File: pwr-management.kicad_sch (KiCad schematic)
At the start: 3 parts, among them U3 BQ297xy, U4 BQ25176JDSGR

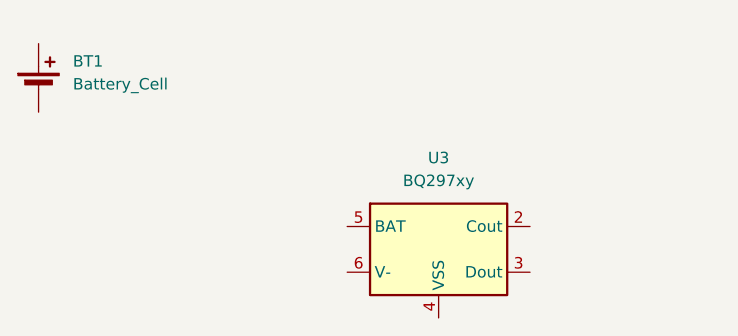
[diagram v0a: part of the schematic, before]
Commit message: component placement inside schematic
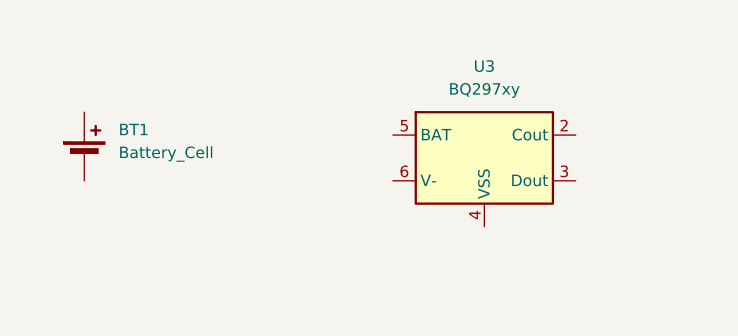
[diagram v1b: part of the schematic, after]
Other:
- moved on the sheet: BT1, U3
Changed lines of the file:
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@@
 	(symbol
 		(lib_id "Battery_Management:BQ297xy")
-		(at 88.9 91.44 0)
+		(at 93.98 81.28 0)
 		(unit 1)
 		(exclude_from_sim no)
@@
 		(fields_autoplaced yes)
 		(property "Reference" "U3"
-			(at 88.9 81.28 0)
+			(at 93.98 71.12 0)
 			(effects
 				(font
@@
 		)
 		(property "Value" "BQ297xy"
-			(at 88.9 83.82 0)
+			(at 93.98 73.66 0)
 			(effects
 				(font
@@
 		)
 		(property "Footprint" "Package_SON:WSON-6_1.5x1.5mm_P0.5mm"
-			(at 88.9 82.55 0)
+			(at 93.98 72.39 0)
 			(effects
 				(font
@@
 		)
 		(property "Datasheet" "http://www.ti.com/lit/ds/symlink/bq2970.pdf"
-			(at 82.55 86.36 0)
+			(at 87.63 76.2 0)
 			(effects
 				(font
@@
 		)
 		(property "Description" "Voltage and Current Protection for Single-Cell Li-Ion and Li-Polymer Batteries"
-			(at 88.9 91.44 0)
+			(at 93.98 81.28 0)
 			(effects
 				(font
@@
 	(symbol
 		(lib_id "Device:Battery_Cell")
-		(at 44.45 73.66 0)
+		(at 49.53 81.28 0)
 		(unit 1)
 		(exclude_from_sim no)
@@
 		(fields_autoplaced yes)
 		(property "Reference" "BT1"
-			(at 48.26 70.5484 0)
+			(at 53.34 78.1684 0)
 			(effects
 				(font
@@
 		)
 		(property "Value" "Battery_Cell"
-			(at 48.26 73.0884 0)
+			(at 53.34 80.7084 0)
 			(effects
 				(font
@@
 		)
 		(property "Footprint" ""
-			(at 44.45 72.136 90)
+			(at 49.53 79.756 90)
 			(effects
 				(font
@@
 		)
 		(property "Datasheet" "~"
-			(at 44.45 72.136 90)
+			(at 49.53 79.756 90)
 			(effects
 				(font
@@
 		)
 		(property "Description" "Single-cell battery"
-			(at 44.45 73.66 0)
+			(at 49.53 81.28 0)
 			(effects
 				(font

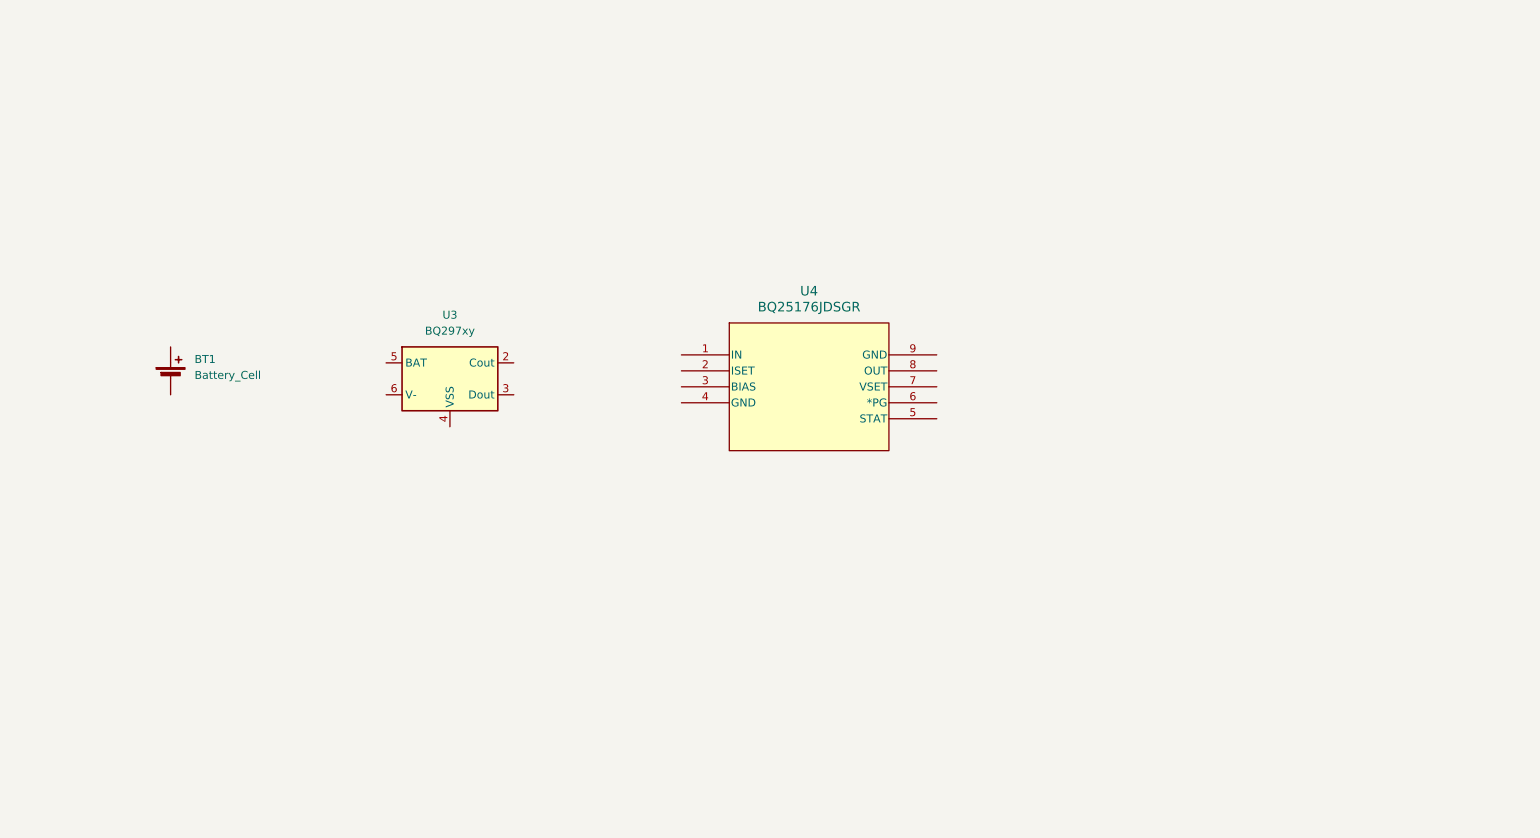
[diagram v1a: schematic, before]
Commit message: fix BQ25176J library
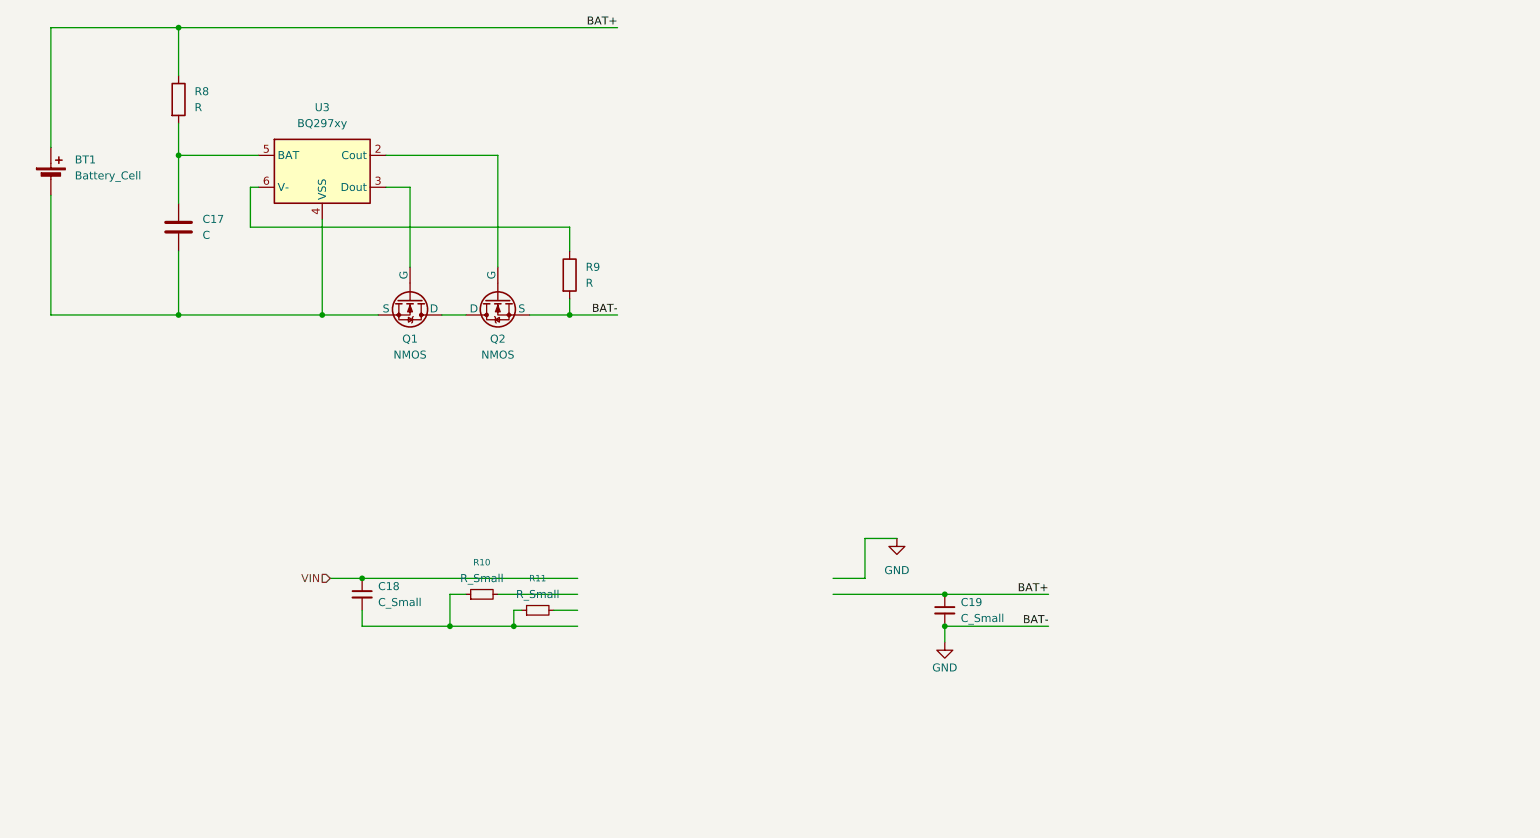
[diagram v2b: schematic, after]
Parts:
- removed U4: BQ25176JDSGR, WSON_MDSGR_TEX, symbol 2025-10-25_14-37-11:BQ25176JDSGR
- added C17: C, symbol Device:C
- added C18, C19: C_Small, symbol Device:C_Small
- added Q1, Q2: NMOS, symbol Simulation_SPICE:NMOS
- added R10, R11: R_Small, symbol Device:R_Small
- added R8, R9: R, symbol Device:R
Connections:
- net at U3.2 (Cout): now also Q2.2 (G)
- net at U3.3 (Dout): now also Q1.2 (G)
- net at U3.4 (VSS): now also BT1.2 (-), C17.2, Q1.3 (S)
- net at U3.5 (BAT): now also C17.1, R8.2
- net at U3.6 (V-): now also R9.1
- net BAT+: now reaches BT1.1 (+)
- net BAT+: now also C19.1, R8.1
- new net: C18.2, R10.1, R11.1
- new net: Q1.1 (D), Q2.1 (D)
- new net GND: C19.2, Q2.3 (S), R9.2
- new net VIN: C18.1
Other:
- moved on the sheet: BT1, U3

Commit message: Add battery handling
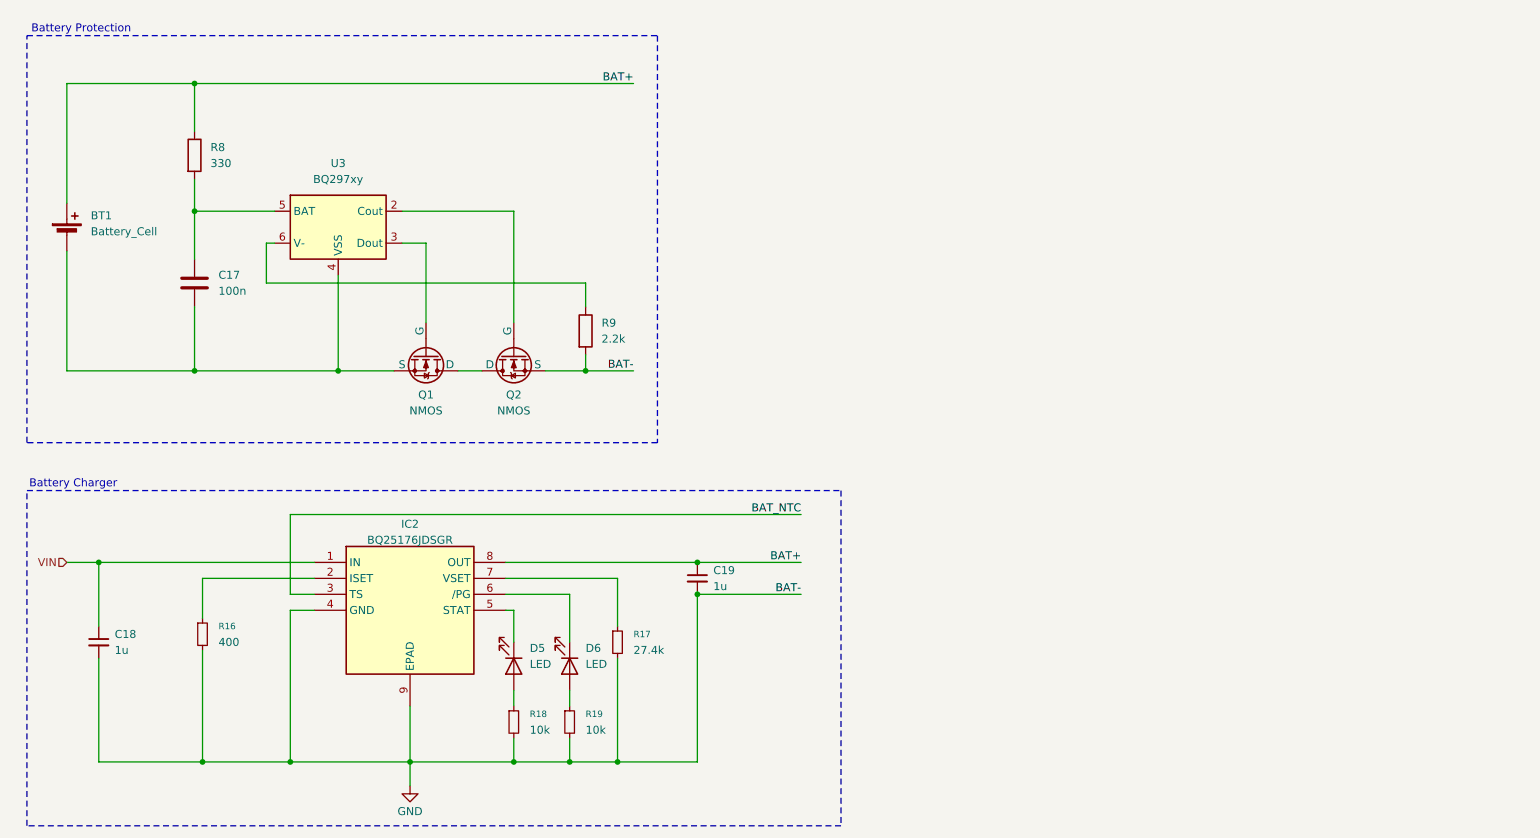
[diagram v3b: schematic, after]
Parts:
- removed R10, R11: R_Small, symbol Device:R_Small
- added D5, D6: LED, symbol Device:LED
- added IC2: BQ25176JDSGR, SON50P200X200X80-9N, symbol BQ25176J:BQ25176JDSGR
- added R16: 400, symbol Device:R_Small
- added R17: 27.4k, symbol Device:R_Small
- added R18, R19: 10k, symbol Device:R_Small
- C17: value C -> 100n
- C18, C19: value C_Small -> 1u
- R8: value R -> 330
- R9: value R -> 2.2k
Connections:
- net BAT+: now also IC2.8 (OUT)
- net GND: now also C18.2, IC2.4 (GND), IC2.9 (EPAD), R16.2, R17.2, R18.2, R19.2
- net VIN: now also IC2.1 (IN)
- new net: IC2.2 (ISET), R16.1
- new net: D5.1 (K), IC2.5 (STAT)
- new net: D6.1 (K), IC2.6 (/PG)
- new net: IC2.7 (VSET), R17.1
- new net: D5.2 (A), R18.1
- new net: D6.2 (A), R19.1
- new net BAT_NTC: IC2.3 (TS)
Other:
- note added: "Battery Charger"
- note added: "Battery Protection"
- moved on the sheet: BT1, C17, C18, C19, Q1, Q2, R8, R9, U3

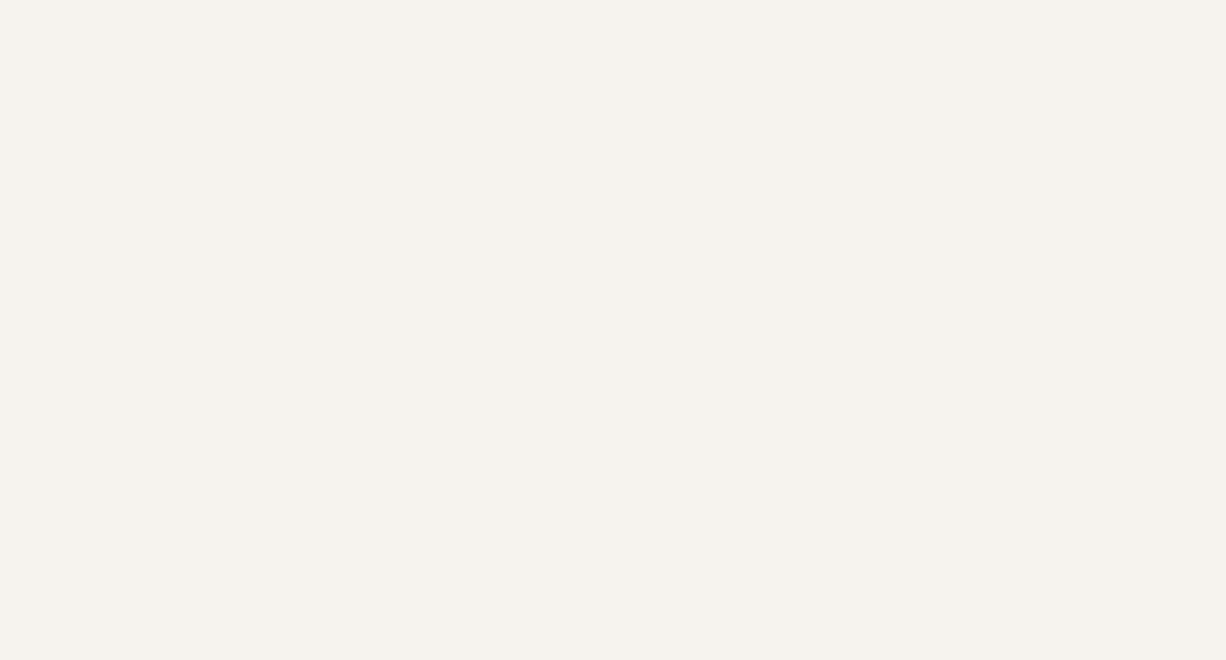
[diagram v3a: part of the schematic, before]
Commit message: add boost converter and ldo regulator
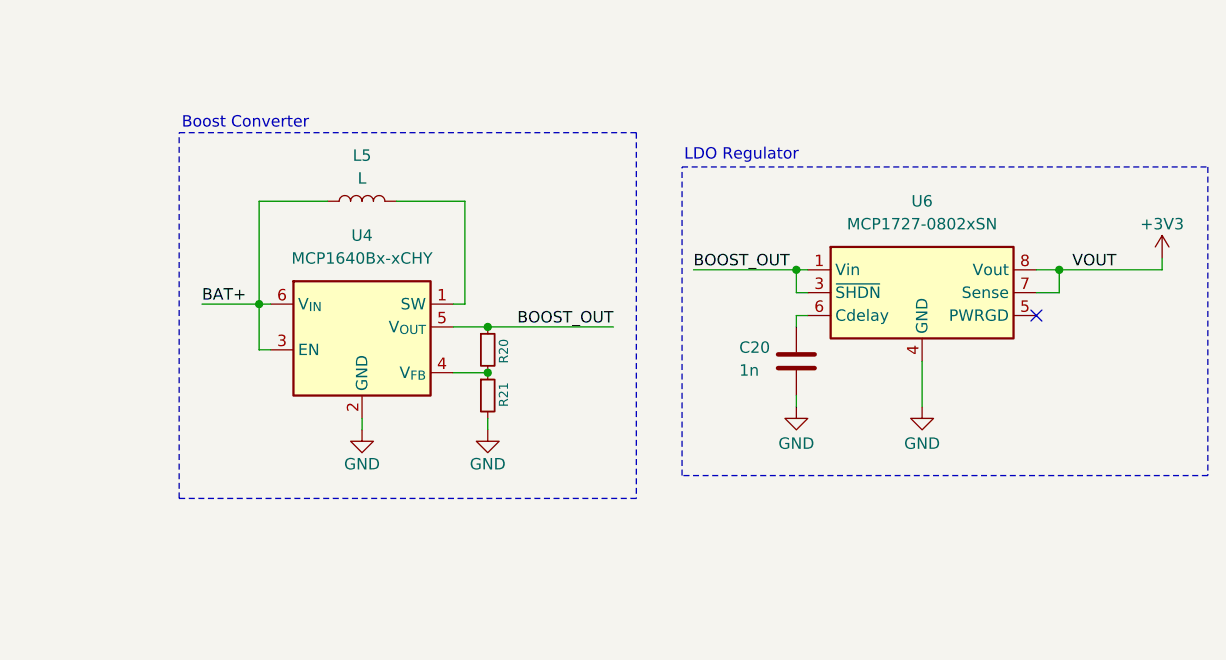
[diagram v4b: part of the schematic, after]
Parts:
- added C20: 1n, symbol Device:C
- added L5: L, symbol Device:L
- added R20, R21: R_Small, symbol Device:R_Small
- added U4: MCP1640Bx-xCHY, Package_TO_SOT_SMD:SOT-23-6, symbol Regulator_Switching:MCP1640Bx-xCHY
- added U6: MCP1727-0802xSN, Package_SO:SOIC-8_3.9x4.9mm_P1.27mm, symbol Regulator_Linear:MCP1727-0802xSN
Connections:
- net BAT+: now also L5.1, U4.3 (EN), U4.6 (V_{IN})
- net GND: now also C20.2, R21.2, U4.2 (GND), U6.4 (GND)
- new net: R20.2, R21.1, U4.4 (V_{FB})
- new net: L5.2, U4.1 (SW)
- new net: C20.1, U6.6 (Cdelay)
- new net +3V3: U6.7 (Sense), U6.8 (Vout)
- new net BOOST_OUT: R20.1, U4.5 (V_{OUT}), U6.1 (Vin), U6.2 (Vin), U6.3 (~{SHDN})
- no-connect marks 0 -> 1
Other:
- note added: "Boost Converter"
- note added: "LDO Regulator"
